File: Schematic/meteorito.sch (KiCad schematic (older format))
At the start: 5 parts, among them P1 DH22, P2 GY-ML8511, P3 BMP180, P4 CONN_01X08, P5 CONN_01X08

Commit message: Agregado wemos lib
Añadido etiquetas de conexión
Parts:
- removed P4, P5: CONN_01X08, Pin_Headers:Pin_Header_Straight_1x08_Pitch2.54mm, symbol CONN_01X08
- added U1: WeMos_mini, symbol WeMos_mini
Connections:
- net labels added: +3.3V, +5V, D3, D5, D6, D7, GND, OUT, RX, SCL, SDA, TX
- wire segments 28 -> 27
- no-connect marks 0 -> 6
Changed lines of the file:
@@
 LIBS:contrib
 LIBS:valves
+LIBS:wemos_mini
 LIBS:meteorito-cache
 EELAYER 25 0
@@
 Sheet 1 1
 Title "MeteoritoBoard"
-Date "2017-07-22"
-Rev "0.1"
+Date "2017-11-02"
+Rev "0.2"
 Comp "ElectronicCats"
 Comment1 "Andres Sabas"
@@
 $EndComp
 $Comp
-L CONN_01X08 P4
-U 1 1 5973BBC7
-P 6765 2825
-F 0 "P4" H 6765 3275 50  0000 C CNN
-F 1 "CONN_01X08" V 6865 2825 50  0000 C CNN
-F 2 "Pin_Headers:Pin_Header_Straight_1x08_Pitch2.54mm" H 6765 2825 50  0001 C CNN
-F 3 "" H 6765 2825 50  0000 C CNN
-	1    6765 2825
-	1    0    0    -1
-$EndComp
-$Comp
-L CONN_01X08 P5
-U 1 1 5973BC14
-P 7255 2820
-F 0 "P5" H 7255 3270 50  0000 C CNN
-F 1 "CONN_01X08" V 7355 2820 50  0000 C CNN
-F 2 "Pin_Headers:Pin_Header_Straight_1x08_Pitch2.54mm" H 7255 2820 50  0001 C CNN
-F 3 "" H 7255 2820 50  0000 C CNN
-	1    7255 2820
-	-1   0    0    -1
-$EndComp
-$Comp
 L CONN_01X05 P2
 U 1 1 5973BC79
@@
 Text Notes 6525 2040 0    60   ~ 0
 Wemos D1 ESP8266
-Wire Wire Line
-	6565 2475 6330 2475
-Wire Wire Line
-	6565 2575 6340 2575
-Wire Wire Line
-	6565 2675 6345 2675
-Wire Wire Line
-	6565 2775 6340 2775
-Wire Wire Line
-	6565 2875 6340 2875
-Wire Wire Line
-	6565 2975 6340 2975
-Wire Wire Line
-	6565 3075 6345 3075
-Wire Wire Line
-	6565 3175 6345 3175
-Wire Wire Line
-	7455 3170 7805 3170
-Wire Wire Line
-	7455 3070 7800 3070
-Wire Wire Line
-	7455 2970 7795 2970
+$Comp
+L WeMos_mini U1
+U 1 1 59FBAE90
+P 6955 2820
+F 0 "U1" H 6955 3320 60  0000 C CNN
+F 1 "WeMos_mini" H 6955 2320 60  0000 C CNN
+F 2 "" H 7505 2120 60  0000 C CNN
+F 3 "" H 7505 2120 60  0000 C CNN
+	1    6955 2820
+	1    0    0    -1
+$EndComp
+$Comp
+L +3.3V #PWR01
+U 1 1 59FBB0B3
+P 7760 2470
+F 0 "#PWR01" H 7760 2320 50  0001 C CNN
+F 1 "+3.3V" H 7760 2610 50  0000 C CNN
+F 2 "" H 7760 2470 50  0000 C CNN
+F 3 "" H 7760 2470 50  0000 C CNN
+	1    7760 2470
+	1    0    0    -1
+$EndComp
+$Comp
+L +5V #PWR02
+U 1 1 59FBB0E7
+P 6220 2470
+F 0 "#PWR02" H 6220 2320 50  0001 C CNN
+F 1 "+5V" H 6220 2610 50  0000 C CNN
+F 2 "" H 6220 2470 50  0000 C CNN
+F 3 "" H 6220 2470 50  0000 C CNN
+	1    6220 2470
+	1    0    0    -1
+$EndComp
+$Comp
+L GND #PWR03
+U 1 1 59FBB107
+P 6120 2580
+F 0 "#PWR03" H 6120 2330 50  0001 C CNN
+F 1 "GND" H 6120 2430 50  0000 C CNN
+F 2 "" H 6120 2580 50  0000 C CNN
+F 3 "" H 6120 2580 50  0000 C CNN
+	1    6120 2580
+	1    0    0    -1
+$EndComp
+Text Label 6230 2770 0    60   ~ 0
+D3
+Text Label 6230 2870 0    60   ~ 0
+SDA
+Text Label 6230 2970 0    60   ~ 0
+SCL
+Text Label 6235 3070 0    60   ~ 0
+RX
+Text Label 7780 2670 0    60   ~ 0
+D7
+Text Label 7790 2770 0    60   ~ 0
+D6
+Text Label 7795 2870 0    60   ~ 0
+D5
+NoConn ~ 7455 3070
+NoConn ~ 7455 3170
+Text Label 6235 3170 0    60   ~ 0
+TX
+Text Label 1920 2035 0    60   ~ 0
+D7
+$Comp
+L +5V #PWR04
+U 1 1 59FBB39C
+P 1930 1835
+F 0 "#PWR04" H 1930 1685 50  0001 C CNN
+F 1 "+5V" H 1930 1975 50  0000 C CNN
+F 2 "" H 1930 1835 50  0000 C CNN
+F 3 "" H 1930 1835 50  0000 C CNN
+	1    1930 1835
+	1    0    0    -1
+$EndComp
+$Comp
+L GND #PWR05
+U 1 1 59FBB3BC
+P 1830 1935
+F 0 "#PWR05" H 1830 1685 50  0001 C CNN
+F 1 "GND" H 1830 1785 50  0000 C CNN
+F 2 "" H 1830 1935 50  0000 C CNN
+F 3 "" H 1830 1935 50  0000 C CNN
+	1    1830 1935
+	1    0    0    -1
+$EndComp
+$Comp
+L GND #PWR06
+U 1 1 59FBB4DC
+P 1890 3260
+F 0 "#PWR06" H 1890 3010 50  0001 C CNN
+F 1 "GND" H 1890 3110 50  0000 C CNN
+F 2 "" H 1890 3260 50  0000 C CNN
+F 3 "" H 1890 3260 50  0000 C CNN
+	1    1890 3260
+	1    0    0    -1
+$EndComp
+$Comp
+L +5V #PWR07
+U 1 1 59FBB563
+P 2040 3155
+F 0 "#PWR07" H 2040 3005 50  0001 C CNN
+F 1 "+5V" H 2040 3295 50  0000 C CNN
+F 2 "" H 2040 3155 50  0000 C CNN
+F 3 "" H 2040 3155 50  0000 C CNN
+	1    2040 3155
+	1    0    0    -1
+$EndComp
+Text Label 2040 3355 0    60   ~ 0
+SCL
+Text Label 2035 3455 0    60   ~ 0
+SDA
+Text Label 2005 5095 0    60   ~ 0
+OUT
+$Comp
+L GND #PWR08
+U 1 1 59FBB69A
+P 1960 5000
+F 0 "#PWR08" H 1960 4750 50  0001 C CNN
+F 1 "GND" H 1960 4850 50  0000 C CNN
+F 2 "" H 1960 5000 50  0000 C CNN
+F 3 "" H 1960 5000 50  0000 C CNN
+	1    1960 5000
+	1    0    0    -1
+$EndComp
+Wire Wire Line
+	6455 2470 6220 2470
+Wire Wire Line
+	6455 2770 6230 2770
+Wire Wire Line
+	6455 2870 6230 2870
+Wire Wire Line
+	6455 2970 6230 2970
+Wire Wire Line
+	6455 3070 6235 3070
+Wire Wire Line
+	6455 3170 6235 3170
 Wire Wire Line
 	7455 2870 7795 2870
 Wire Wire Line
 	7455 2470 7760 2470
-Wire Wire Line
-	7455 2570 7770 2570
 Wire Wire Line
 	7455 2670 7780 2670
@@
 	2145 1835 1930 1835
 Wire Wire Line
-	2145 1935 1925 1935
+	1830 1935 2145 1935
 Wire Wire Line
 	2145 2035 1920 2035
@@
 	2185 3155 2040 3155
 Wire Wire Line
-	2185 3255 2040 3255
+	1890 3255 2185 3255
 Wire Wire Line
 	2185 3355 2040 3355
@@
 	2155 4795 2015 4795
 Wire Wire Line
-	2155 4895 2010 4895
-Wire Wire Line
-	2155 4995 2010 4995
+	1960 4995 2155 4995
 Wire Wire Line
 	2155 5095 2005 5095
 Wire Wire Line
 	2155 5195 2005 5195
+Wire Wire Line
+	6120 2570 6120 2580
+Wire Wire Line
+	6120 2570 6455 2570
+Wire Wire Line
+	1890 3255 1890 3260
+$Comp
+L +3.3V #PWR09
+U 1 1 59FBB72C
+P 1815 5330
+F 0 "#PWR09" H 1815 5180 50  0001 C CNN
+F 1 "+3.3V" H 1815 5470 50  0000 C CNN
+F 2 "" H 1815 5330 50  0000 C CNN
+F 3 "" H 1815 5330 50  0000 C CNN
+	1    1815 5330
+	1    0    0    -1
+$EndComp
+Wire Wire Line
+	1815 5335 2005 5335
+Wire Wire Line
+	2005 5335 2005 5195
+Wire Wire Line
+	1960 4995 1960 5000
+$Comp
+L +5V #PWR010
+U 1 1 59FBB879
+P 2015 4795
+F 0 "#PWR010" H 2015 4645 50  0001 C CNN
+F 1 "+5V" H 2015 4935 50  0000 C CNN
+F 2 "" H 2015 4795 50  0000 C CNN
+F 3 "" H 2015 4795 50  0000 C CNN
+	1    2015 4795
+	1    0    0    -1
+$EndComp
+NoConn ~ 2155 4895
+NoConn ~ 7455 2570
+NoConn ~ 7455 2970
+NoConn ~ 6455 2670
 $EndSCHEMATC

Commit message: Update conectores
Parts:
- removed U1: WeMos_mini, symbol WeMos_mini
- added P?: Hall, symbol CONN_01X03
- added P? (x4): CONN_01X10, symbol CONN_01X10
- added R?: FOTORESISTENCIA, symbol R_Small
- added R?: 100, symbol R_Small
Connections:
- net labels added: D13
- wire segments 27 -> 36
- no-connect marks 6 -> 4
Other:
- note added: "HUMEDAD y TEMPERATURA"
- note added: "NUBOSIDAD"
- note added: "PRESION ATMOSFERICA"
- note added: "UV"
- note added: "VELOCIDAD DEL AIRE"
- note added: "Wemos D1 ESP32"
- note removed: "Wemos D1 ESP8266"
- moved on the sheet: P1, P2, P3

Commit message: Se agregaron dos sensores de efecto Hall
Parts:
- added P? (x2): Hall, symbol meteorito-rescue:CONN_01X03
- P1, P?: symbol CONN_01X03 -> meteorito-rescue:CONN_01X03
- P2: symbol CONN_01X05 -> meteorito-rescue:CONN_01X05
- P3: symbol CONN_01X04 -> meteorito-rescue:CONN_01X04
- P? (x4): symbol CONN_01X10 -> meteorito-rescue:CONN_01X10
- R? (x2): symbol R_Small -> Device:R_Small
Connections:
- wire segments 36 -> 41
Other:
- note added: "Sensores Efecto Hall\n"
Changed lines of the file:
@@
-EESchema Schematic File Version 2
-LIBS:power
-LIBS:device
-LIBS:transistors
-LIBS:conn
-LIBS:linear
-LIBS:regul
-LIBS:74xx
-LIBS:cmos4000
-LIBS:adc-dac
-LIBS:memory
-LIBS:xilinx
-LIBS:microcontrollers
-LIBS:dsp
-LIBS:microchip
-LIBS:analog_switches
-LIBS:motorola
-LIBS:texas
-LIBS:intel
-LIBS:audio
-LIBS:interface
-LIBS:digital-audio
-LIBS:philips
-LIBS:display
-LIBS:cypress
-LIBS:siliconi
-LIBS:opto
-LIBS:atmel
-LIBS:contrib
-LIBS:valves
-LIBS:wemos_mini
+EESchema Schematic File Version 4
 LIBS:meteorito-cache
-EELAYER 25 0
+EELAYER 26 0
 EELAYER END
 $Descr A4 11693 8268
@@
 $EndDescr
 $Comp
-L CONN_01X04 P3
+L meteorito-rescue:CONN_01X04 P3
 U 1 1 5973B1FD
 P 2370 2400
@@
 $EndComp
 $Comp
-L CONN_01X05 P2
+L meteorito-rescue:CONN_01X05 P2
 U 1 1 5973BC79
 P 2300 3875
@@
 D7
 $Comp
-L GND #PWR06
+L power:GND #PWR06
 U 1 1 59FBB4DC
 P 1875 2355
@@
 $EndComp
 $Comp
-L +5V #PWR07
+L power:+5V #PWR07
 U 1 1 59FBB563
 P 2025 2250
@@
 SDA
 $Comp
-L GND #PWR08
+L power:GND #PWR08
 U 1 1 59FBB69A
 P 1905 3880
@@
 $EndComp
 $Comp
-L +5V #PWR010
+L power:+5V #PWR010
 U 1 1 59FBB879
 P 1960 3675
@@
 NoConn ~ 2100 3775
 $Comp
-L +5V #PWR04
+L power:+5V #PWR04
 U 1 1 59FBB39C
 P 1860 995
@@
 $EndComp
 $Comp
-L GND #PWR05
+L power:GND #PWR05
 U 1 1 59FBB3BC
 P 1760 1095
@@
 Wemos D1 ESP32
 $Comp
-L CONN_01X03 P1
+L meteorito-rescue:CONN_01X03 P1
 U 1 1 5973B1A0
 P 2275 1095
@@
 $EndComp
 $Comp
-L CONN_01X03 P?
+L meteorito-rescue:CONN_01X03 P?
 U 1 1 5B3AB6AA
 P 2325 5120
@@
 $EndComp
 $Comp
-L +5V #PWR?
+L power:+5V #PWR?
 U 1 1 5B3ABCF3
 P 1760 4215
@@
 OUT
 $Comp
-L R_Small R?
+L Device:R_Small R?
 U 1 1 5B3ABF7D
 P 1900 6565
@@
 $EndComp
 $Comp
-L R_Small R?
+L Device:R_Small R?
 U 1 1 5B3AC023
 P 1900 6850
@@
 $EndComp
 $Comp
-L GND #PWR?
+L power:GND #PWR?
 U 1 1 5B3AC2DB
 P 1900 7050
@@
 D13
 $Comp
-L +3.3V #PWR?
+L power:+3.3V #PWR?
 U 1 1 5B3AC40A
 P 1900 6370
@@
 $EndComp
 $Comp
-L GND #PWR?
+L power:GND #PWR?
 U 1 1 5B3AC68F
 P 1975 5220
@@
 $EndComp
 $Comp
-L CONN_01X10 P?
+L meteorito-rescue:CONN_01X10 P?
 U 1 1 5B3ACF92
 P 7335 2260
@@
 $EndComp
 $Comp
-L CONN_01X10 P?
+L meteorito-rescue:CONN_01X10 P?
 U 1 1 5B3AD073
 P 6535 2265
@@
 $EndComp
 $Comp
-L CONN_01X10 P?
+L meteorito-rescue:CONN_01X10 P?
 U 1 1 5B3AD0C5
 P 7935 2260
@@
 $EndComp
 $Comp
-L CONN_01X10 P?
+L meteorito-rescue:CONN_01X10 P?
 U 1 1 5B3AD12E
 P 8780 2240
@@
 	8135 2110 8470 2110
 Wire Notes Line
-	4315 515  4315 7755
-Wire Notes Line
 	4315 4065 11215 4065
 Wire Notes Line
@@
 	2125 5220 1975 5220
 Wire Wire Line
-	1900 6665 1900 6750
+	1900 6665 1900 6710
 Wire Wire Line
 	1900 6710 2115 6710
@@
 	1900 6950 1900 7050
 Wire Notes Line
-	4305 4260 11220 4260
+	4305 5460 11220 5460
 Wire Notes Line
 	11220 4260 11220 4250
@@
 Wire Notes Line
 	465  5740 4315 5740
-Wire Notes Line
-	4315 5740 4315 5755
 Text Notes 1915 5915 0    60   ~ 0
 NUBOSIDAD
 Text Label 8260 2315 0    60   ~ 0
 OUT
+Wire Wire Line
+	1900 6710 1900 6750
+Wire Notes Line
+	4315 515  4315 7755
+$Comp
+L meteorito-rescue:CONN_01X03 P?
+U 1 1 5B9C70A3
+P 5300 4750
+F 0 "P?" H 5300 4950 50  0000 C CNN
+F 1 "Hall" V 5400 4750 50  0000 C CNN
+F 2 "" H 5300 4750 50  0000 C CNN
+F 3 "" H 5300 4750 50  0000 C CNN
+	1    5300 4750
+	1    0    0    -1
+$EndComp
+$Comp
+L power:GND #PWR?
+U 1 1 5B9C7410
+P 4900 5100
+F 0 "#PWR?" H 4900 4850 50  0001 C CNN
+F 1 "GND" H 4905 4927 50  0000 C CNN
+F 2 "" H 4900 5100 50  0001 C CNN
+F 3 "" H 4900 5100 50  0001 C CNN
+	1    4900 5100
+	1    0    0    -1
+$EndComp
+Wire Wire Line
+	5100 4850 4900 4850
+Wire Wire Line
+	4900 4850 4900 5100
+$Comp
+L meteorito-rescue:CONN_01X03 P?
+U 1 1 5B9C7F56
+P 6500 4750
+F 0 "P?" H 6500 4950 50  0000 C CNN
+F 1 "Hall" V 6600 4750 50  0000 C CNN
+F 2 "" H 6500 4750 50  0000 C CNN
+F 3 "" H 6500 4750 50  0000 C CNN
+	1    6500 4750
+	1    0    0    -1
+$EndComp
+$Comp
+L power:GND #PWR?
+U 1 1 5B9C7FC0
+P 6150 5150
+F 0 "#PWR?" H 6150 4900 50  0001 C CNN
+F 1 "GND" H 6155 4977 50  0000 C CNN
+F 2 "" H 6150 5150 50  0001 C CNN
+F 3 "" H 6150 5150 50  0001 C CNN
+	1    6150 5150
+	1    0    0    -1
+$EndComp
+Wire Wire Line
+	6150 5150 6150 4850
+Wire Wire Line
+	6150 4850 6300 4850
+Text Notes 5300 4200 0    50   ~ 0
+Sensores Efecto Hall\n
+Wire Notes Line
+	7150 4050 7150 5450
 $EndSCHEMATC

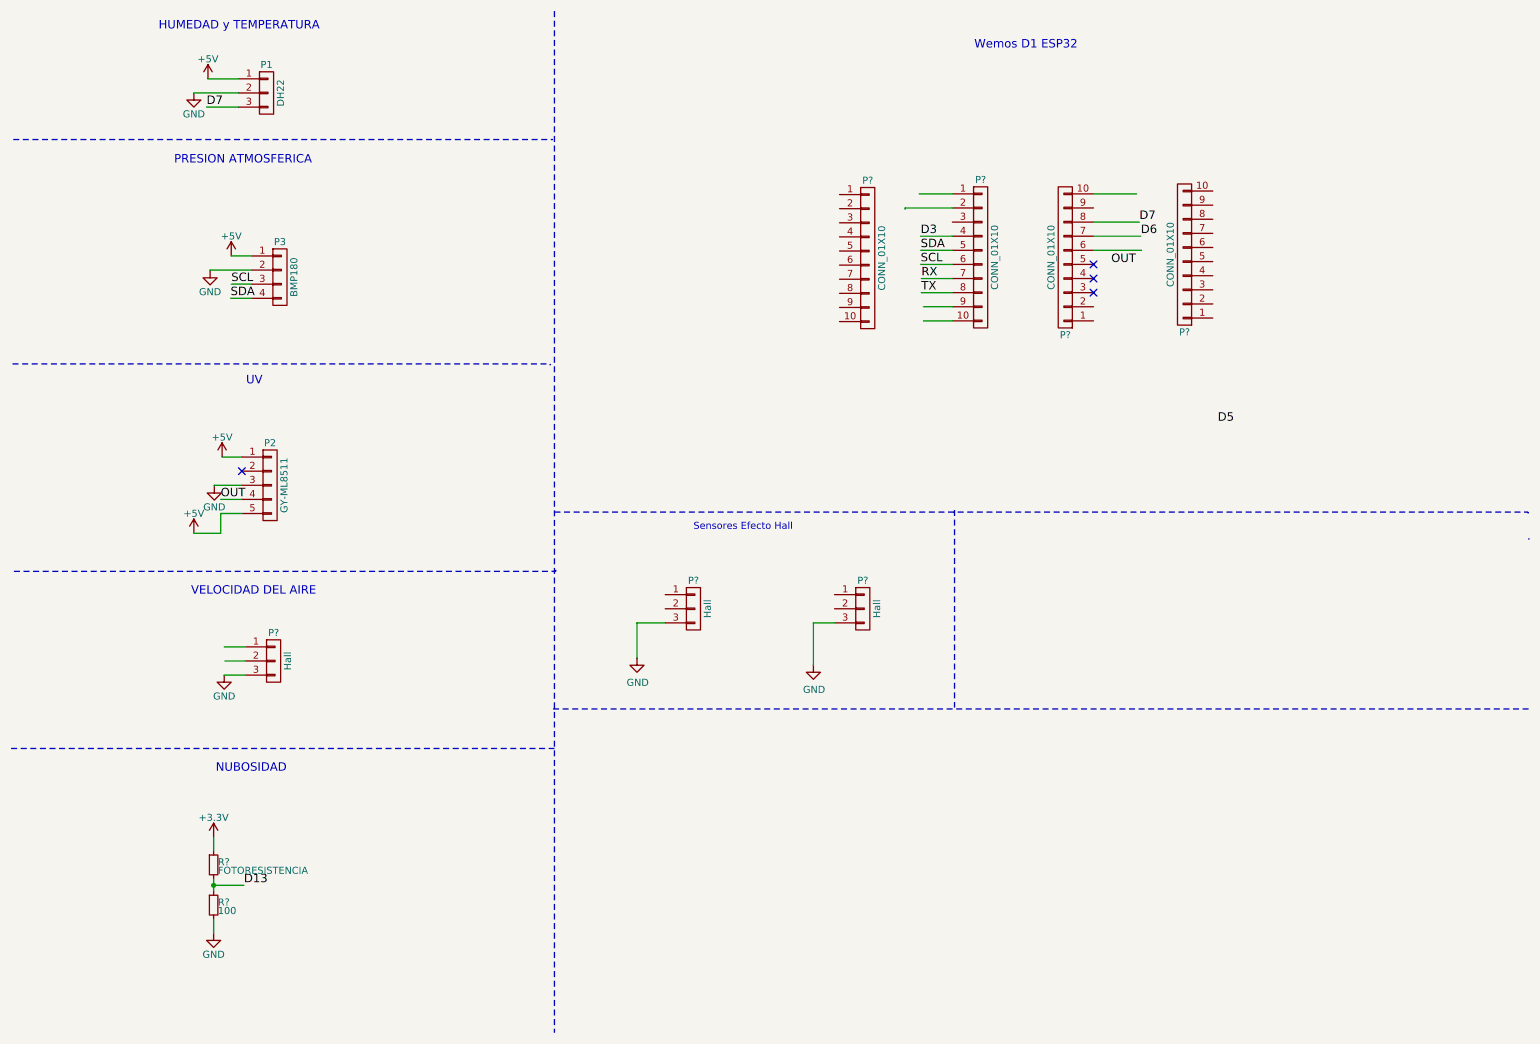
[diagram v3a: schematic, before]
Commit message: Cambios
Se cambiaron errores que tenían algunos sensores y se asignaron etiquetas a los pines
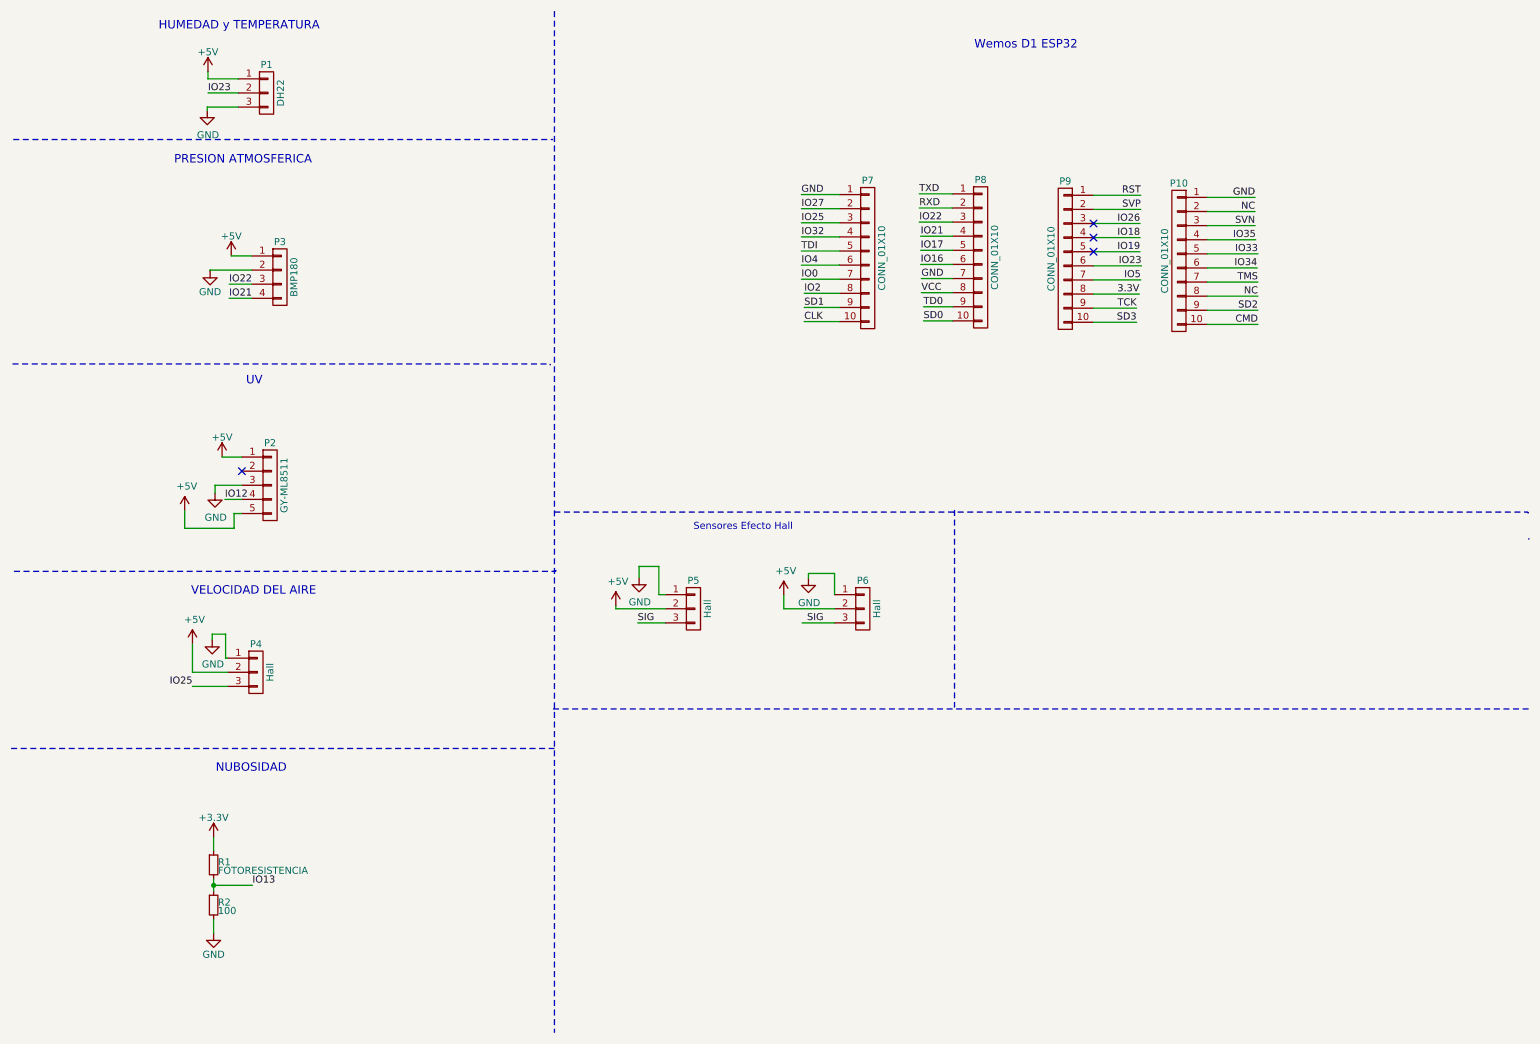
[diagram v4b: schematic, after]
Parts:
- removed P?: Hall, symbol meteorito-rescue:CONN_01X03
- added P4: Hall, symbol meteorito-rescue:CONN_01X03
- gave numbers to parts that had none: 8
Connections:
- net labels added: 3.3V, CLK, CMD, IO0, IO12, IO13, IO16, IO17, IO18, IO19, IO2, IO21, IO22, IO23, IO25, IO26, IO27, IO32, IO33, IO34, IO35, IO4, IO5, NC, RST, RXD, SD0, SD1, SD2, SD3, SIG, SVN, SVP, TCK, TD0, TDI, TMS, TXD, VCC
- net labels removed: D13, D3, D5, D6, D7, OUT, RX, SCL, SDA, TX
- wire segments 41 -> 83
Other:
- moved on the sheet: P10
